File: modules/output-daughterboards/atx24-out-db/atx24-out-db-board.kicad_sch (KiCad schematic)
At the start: 11 parts, among them J1 ATX24 OUT FIELD, J10 TE 63849-1, J11 TE 63849-1, J12 TE 63849-1, J13 TE 63849-1, J14 TE 63849-1, J15 TE 63849-1, J16 TE 63849-1, J17 TE 63849-1, J18 TE 63849-1, J20 SIGNAL STUB (2x5)

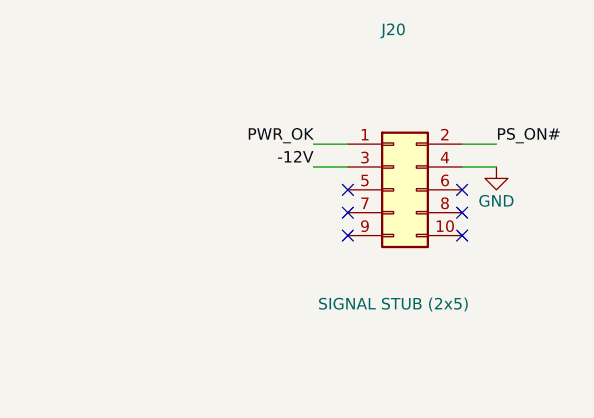
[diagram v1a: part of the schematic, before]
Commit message: Task 10: output-daughterboard projects landed (atx24/eps/pcie, SS2.8 v1.4.0)
Three passive per-cable boards: TE 63849-1 tabs mapped 1:1 to the main
boards' TB order (a pin swap caught+fixed by cross-ref), full TH output
fields (24-circuit ATX / EPS 4+4 / PCIe 3+3+2sense-tied-GND), asymmetric
keying verified programmatically distinct across families, M3 chassis
mounts. 4-layer 2oz: EPS/PCIe = zero-track pure-pour 2-net boards; atx24 =
8-net In2 band routing (stale-netlist silent-reassignment bug found+fixed).
ERC 0 errors / DRC 0 at every severity, netlist-verified by
check_output_daughterboards.py. MODDIY not invented (OQ-88 provenance);
sense-return provisioned only (box e open). New lib assets + parametric
generator + check script.

Co-Authored-By: Claude Fable 5 <noreply@anthropic.com>
Claude-Session: https://claude.ai/code/session_01LvfqcnEeuin2oyJQw548EX
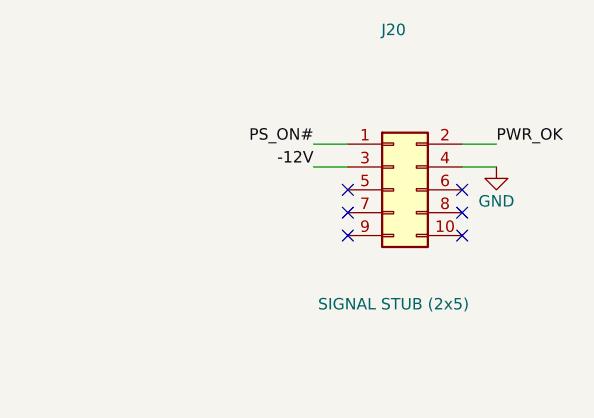
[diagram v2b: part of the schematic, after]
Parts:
- J1: Manufacturer (none) -> CEC (in-house)
- J10, J11, J12, J13, J14, J15, J16, J17, J18: LCSC (none) -> C86469; MPN (none) -> 63849-1; Manufacturer (none) -> TE Connectivity
- J20: Manufacturer (none) -> generic
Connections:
- net PS_ON#: now also J20.1 (Pin_1); no longer J20.2 (Pin_2)
- net PWR_OK: now also J20.2 (Pin_2); no longer J20.1 (Pin_1)

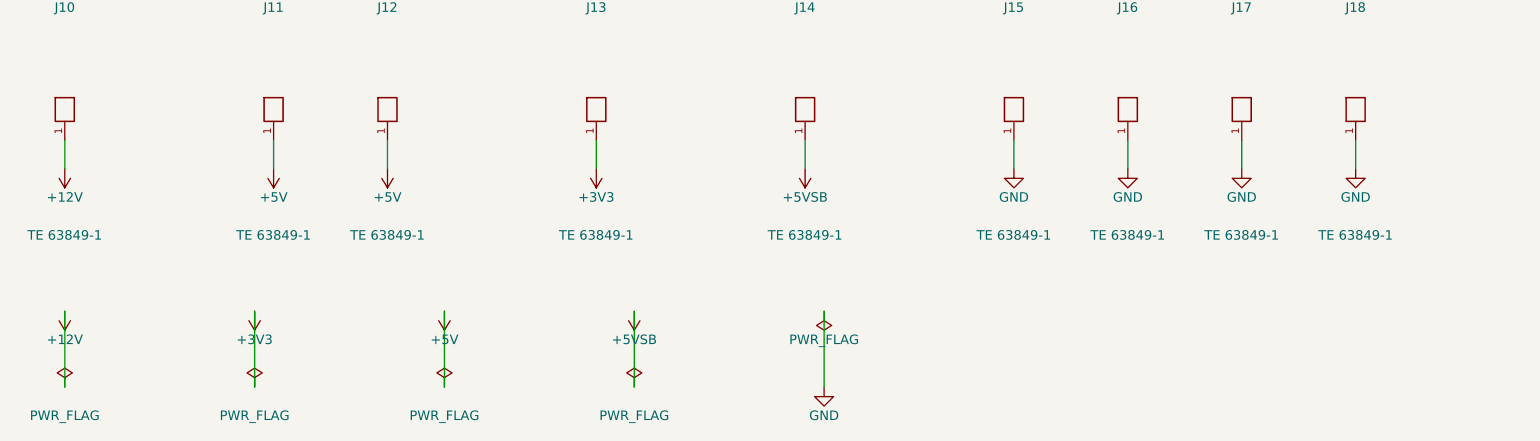
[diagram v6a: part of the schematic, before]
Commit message: WIP snapshot: flat-tab agent regenerating daughterboards onto TE 63951-1 (durability; verification pending)
Co-Authored-By: Claude Fable 5 <noreply@anthropic.com>
Claude-Session: https://claude.ai/code/session_01LvfqcnEeuin2oyJQw548EX
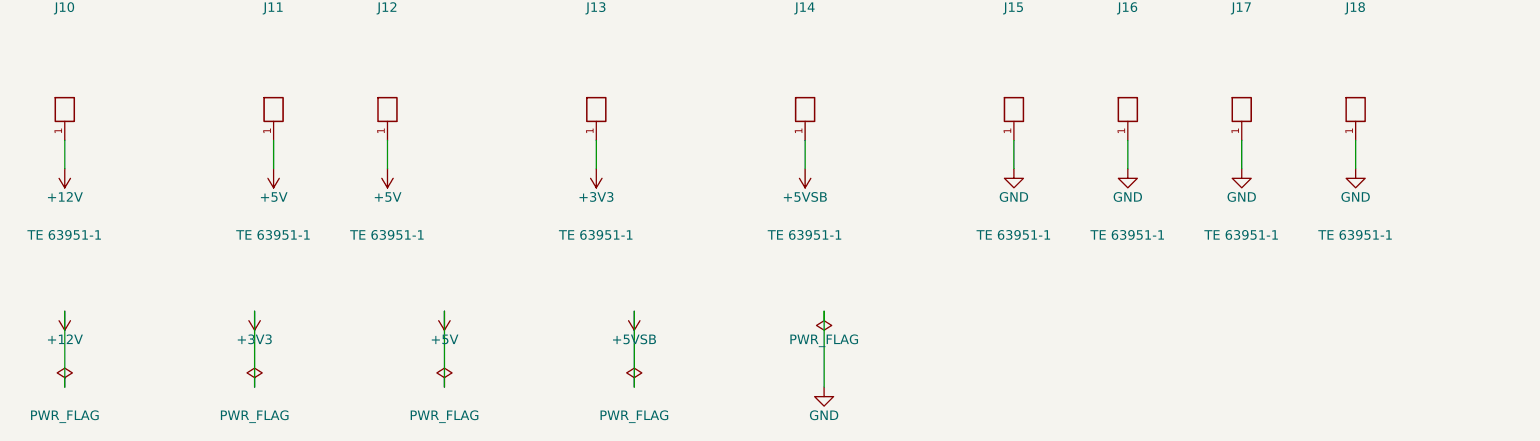
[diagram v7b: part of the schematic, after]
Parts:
- removed J10, J11, J12, J13, J14, J15, J16, J17, J18: TE 63849-1, cec-Connector_Blade:TE_63849-1_FASTON_Tab_250x032_THT, symbol cec-vendor:TE_63849-1_FASTON_Tab
- added J10, J11, J12, J13, J14, J15, J16, J17, J18: TE 63951-1, cec-Connector_Blade:TE_63951-1_FASTON_Tab_250x032_RA_THT, symbol cec-vendor:TE_63951-1_FASTON_Tab
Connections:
- net +12V: now also J10.1
- net +3V3: now also J13.1
- net +5V: now also J11.1, J12.1
- net +5VSB: now also J14.1
- net GND: now also J15.1, J16.1, J17.1, J18.1
